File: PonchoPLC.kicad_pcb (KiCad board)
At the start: 2 copper layers, 85.7 x 137.2 mm, 137 parts, among them J1 I2C, J10 TB_1X3, J11 TB_1X3, J2 RS-232, J3 TB_1X3, J4 TB_1X3, J5 TB_1X2, J6 TB_1X2, J7 TB_1X2, J8 TB_1X3, J9 TB_1X3, K1 RELAY_C, K2 RELAY_C, K3 RELAY_C, K4 RELAY_C, P1 CONN_02X20, P10 CONN_01X20, P11 CONN_01X20, P12 CONN_01X06, P13 CONN_01X06, P14 CONN_02X12, P15 CONN_02X12, P16 CONN_02X12, P17 CONN_02X12, P18 CONN_01X12, P19 CONN_01X12, P2 CONN_01X20, P20 CONN_01X12, P21 CONN_01X12, P3 CONN_02X20, P4 CONN_02X20, P5 CONN_01X19, P6 CONN_02X20, P7 CONN_01X20, P8 CONN_02X20, P9 CONN_02X20, Q1 FQT13N06L, Q2 FQT13N06L, Q3 FQT13N06L, Q4 FQT13N06L, Q5 2N7002, Q6 2N7002, Q7 2N7002, Q8 2N7002, U1 TLP627-4, U2 TLP627-4, U3 MCP1416, U4 MCP1416, U5 MCP1416, U6 MCP1416

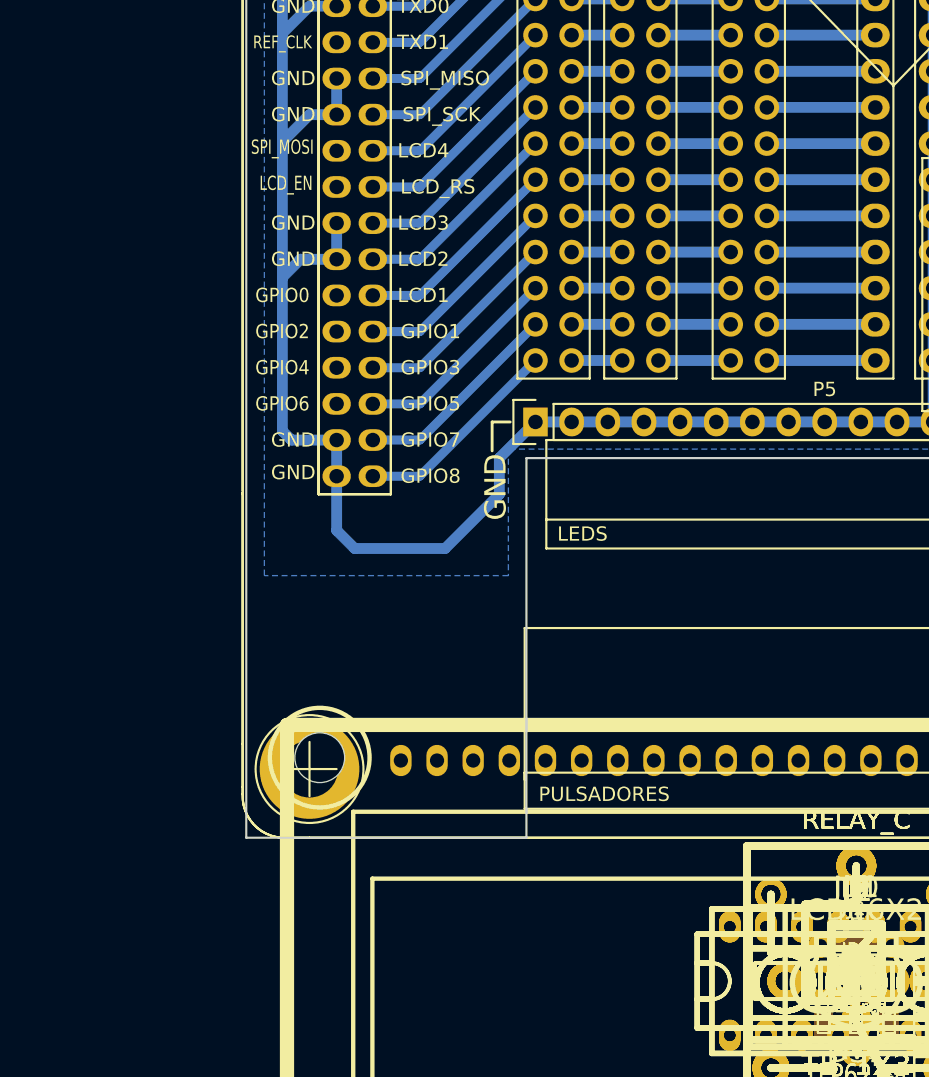
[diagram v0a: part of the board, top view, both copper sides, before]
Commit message: Librería de footprint del proyecto
Generación de la librería de footprint propia del proyecto.
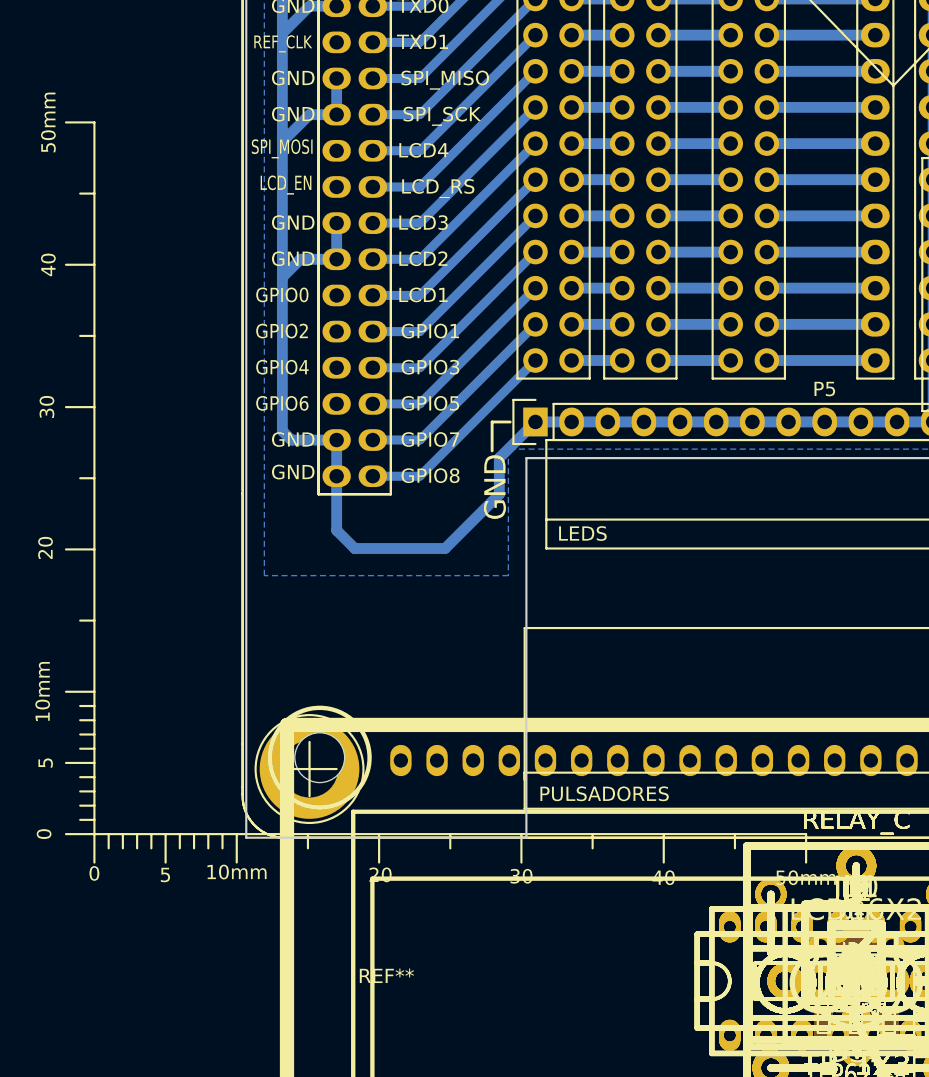
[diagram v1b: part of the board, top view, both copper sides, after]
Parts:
- added REF**: Gauge_50mm_Type2_SilkScreenTop, Measurement_Scales:Gauge_50mm_Type2_SilkScreenTop, F.Cu at (63.0, 162.3)
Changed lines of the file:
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@@
-(kicad_pcb (version 4) (host pcbnew 4.0.1-stable)
+(kicad_pcb (version 4) (host pcbnew 4.0.2-stable)
   (general
     (links 539)
@@
     (tracks 437)
     (zones 0)
-    (modules 137)
+    (modules 138)
     (nets 324)
   )
@@
     )
   )
+  (module Measurement_Scales:Gauge_50mm_Type2_SilkScreenTop (layer F.Cu)
+    (at 62.992 162.306)
+    (descr "Gauge, Massstab, 50mm, SilkScreenTop, Type 2,")
+    (tags "Gauge, Massstab, 50mm, SilkScreenTop, Type 2,")
+    (fp_text reference REF** (at 20.50034 9.99998) (layer F.SilkS)
+      (effects (font (size 1 1) (thickness 0.15)))
+    )
+    (fp_text value Gauge_50mm_Type2_SilkScreenTop (at 24.00046 6.4008) (layer F.Fab)
+      (effects (font (size 1 1) (thickness 0.15)))
+    )
+    (fp_text user 10mm (at -3.59918 -10.00252 90) (layer F.SilkS)
+      (effects (font (size 1 1) (thickness 0.15)))
+    )
+    (fp_text user 0 (at -3.50012 -0.00254 90) (layer F.SilkS)
+      (effects (font (size 1 1) (thickness 0.15)))
+    )
+    (fp_text user 5 (at -3.39852 -5.00126 90) (layer F.SilkS)
+      (effects (font (size 1 1) (thickness 0.15)))
+    )
+    (fp_text user 20 (at -3.39852 -20.10156 90) (layer F.SilkS)
+      (effects (font (size 1 1) (thickness 0.15)))
+    )
+    (fp_text user 30 (at -3.29946 -30.00248 90) (layer F.SilkS)
+      (effects (font (size 1 1) (thickness 0.15)))
+    )
+    (fp_text user 40 (at -3.19786 -40.00246 90) (layer F.SilkS)
+      (effects (font (size 1 1) (thickness 0.15)))
+    )
+    (fp_text user 50mm (at -3.19786 -50.00244 90) (layer F.SilkS)
+      (effects (font (size 1 1) (thickness 0.15)))
+    )
+    (fp_line (start 0 -45.00118) (end -1.00076 -45.00118) (layer F.SilkS) (width 0.15))
+    (fp_line (start 0 -39.99992) (end -1.99898 -39.99992) (layer F.SilkS) (width 0.15))
+    (fp_line (start 0 -35.0012) (end -1.00076 -35.0012) (layer F.SilkS) (width 0.15))
+    (fp_line (start 0 -29.99994) (end -1.99898 -29.99994) (layer F.SilkS) (width 0.15))
+    (fp_line (start 0 -25.00122) (end -1.00076 -25.00122) (layer F.SilkS) (width 0.15))
+    (fp_line (start 0 -19.99996) (end -1.99898 -19.99996) (layer F.SilkS) (width 0.15))
+    (fp_line (start 0 -15.00124) (end -1.00076 -15.00124) (layer F.SilkS) (width 0.15))
+    (fp_line (start 0 -8.99922) (end -1.00076 -8.99922) (layer F.SilkS) (width 0.15))
+    (fp_line (start 0 -8.001) (end -1.00076 -8.001) (layer F.SilkS) (width 0.15))
+    (fp_line (start 0 -7.00024) (end -1.00076 -7.00024) (layer F.SilkS) (width 0.15))
+    (fp_line (start 0 -5.99948) (end -1.00076 -5.99948) (layer F.SilkS) (width 0.15))
+    (fp_line (start 0 -9.99998) (end -1.99898 -9.99998) (layer F.SilkS) (width 0.15))
+    (fp_line (start 0 -4.0005) (end -1.00076 -4.0005) (layer F.SilkS) (width 0.15))
+    (fp_line (start 0 -2.99974) (end -1.00076 -2.99974) (layer F.SilkS) (width 0.15))
+    (fp_line (start 0 -1.99898) (end -1.00076 -1.99898) (layer F.SilkS) (width 0.15))
+    (fp_line (start 0 -1.00076) (end -1.00076 -1.00076) (layer F.SilkS) (width 0.15))
+    (fp_line (start 0 -5.00126) (end -1.99898 -5.00126) (layer F.SilkS) (width 0.15))
+    (fp_line (start 0 0) (end -1.99898 0) (layer F.SilkS) (width 0.15))
+    (fp_line (start 0 -49.9999) (end -1.99898 -49.9999) (layer F.SilkS) (width 0.15))
+    (fp_line (start 0 0) (end 0 -49.9999) (layer F.SilkS) (width 0.15))
+    (fp_line (start 9.99998 0) (end 49.9999 0) (layer F.SilkS) (width 0.15))
+    (fp_text user 50mm (at 49.9999 3.10134) (layer F.SilkS)
+      (effects (font (size 1 1) (thickness 0.15)))
+    )
+    (fp_text user 40 (at 39.99992 3.10134) (layer F.SilkS)
+      (effects (font (size 1 1) (thickness 0.15)))
+    )
+    (fp_text user 30 (at 29.99994 2.99974) (layer F.SilkS)
+      (effects (font (size 1 1) (thickness 0.15)))
+    )
+    (fp_text user 20 (at 20.09902 2.90068) (layer F.SilkS)
+      (effects (font (size 1 1) (thickness 0.15)))
+    )
+    (fp_line (start 49.9999 0) (end 49.9999 1.99898) (layer F.SilkS) (width 0.15))
+    (fp_line (start 45.00118 0) (end 45.00118 1.00076) (layer F.SilkS) (width 0.15))
+    (fp_line (start 39.99992 0) (end 39.99992 1.99898) (layer F.SilkS) (width 0.15))
+    (fp_line (start 35.0012 0) (end 35.0012 1.00076) (layer F.SilkS) (width 0.15))
+    (fp_line (start 29.99994 0) (end 29.99994 1.99898) (layer F.SilkS) (width 0.15))
+    (fp_line (start 25.00122 0) (end 25.00122 1.00076) (layer F.SilkS) (width 0.15))
+    (fp_line (start 19.99996 0) (end 19.99996 1.99898) (layer F.SilkS) (width 0.15))
+    (fp_line (start 15.00124 0) (end 15.00124 1.00076) (layer F.SilkS) (width 0.15))
+    (fp_text user 5 (at 4.99872 2.90068) (layer F.SilkS)
+      (effects (font (size 1 1) (thickness 0.15)))
+    )
+    (fp_text user 0 (at 0 2.79908) (layer F.SilkS)
+      (effects (font (size 1 1) (thickness 0.15)))
+    )
+    (fp_text user 10mm (at 9.99998 2.70002) (layer F.SilkS)
+      (effects (font (size 1 1) (thickness 0.15)))
+    )
+    (fp_line (start 8.99922 0) (end 8.99922 1.00076) (layer F.SilkS) (width 0.15))
+    (fp_line (start 8.001 0) (end 8.001 1.00076) (layer F.SilkS) (width 0.15))
+    (fp_line (start 7.00024 0) (end 7.00024 1.00076) (layer F.SilkS) (width 0.15))
+    (fp_line (start 5.99948 0) (end 5.99948 1.00076) (layer F.SilkS) (width 0.15))
+    (fp_line (start 4.0005 0) (end 4.0005 1.00076) (layer F.SilkS) (width 0.15))
+    (fp_line (start 2.99974 0) (end 2.99974 1.00076) (layer F.SilkS) (width 0.15))
+    (fp_line (start 1.99898 0) (end 1.99898 1.00076) (layer F.SilkS) (width 0.15))
+    (fp_line (start 1.00076 0) (end 1.00076 1.00076) (layer F.SilkS) (width 0.15))
+    (fp_line (start 5.00126 0) (end 5.00126 1.99898) (layer F.SilkS) (width 0.15))
+    (fp_line (start 0 0) (end 0 1.99898) (layer F.SilkS) (width 0.15))
+    (fp_line (start 0 0) (end 9.99998 0) (layer F.SilkS) (width 0.15))
+    (fp_line (start 9.99998 0) (end 9.99998 1.99898) (layer F.SilkS) (width 0.15))
+  )
   (dimension 85.725 (width 0.3) (layer Dwgs.User)
